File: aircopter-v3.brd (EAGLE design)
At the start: 47 x 28 mm, 44 parts, among them IC1 STF202-22T1G, M1 WIRELESS-NRF24L01, U2 GY-521MPU6050, Y1 20 MHz

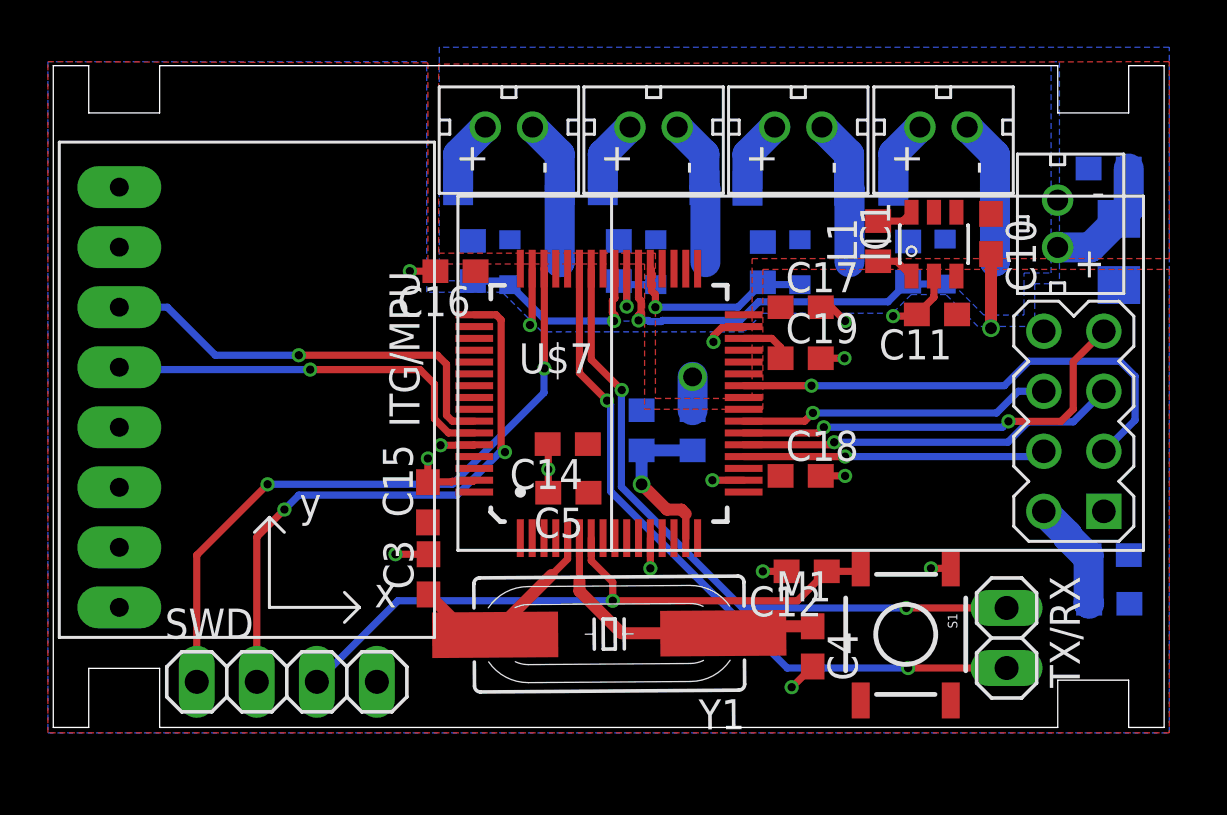
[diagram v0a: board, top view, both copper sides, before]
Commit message: redid motor section and planes, slightly moved mcu and radio, other small changes
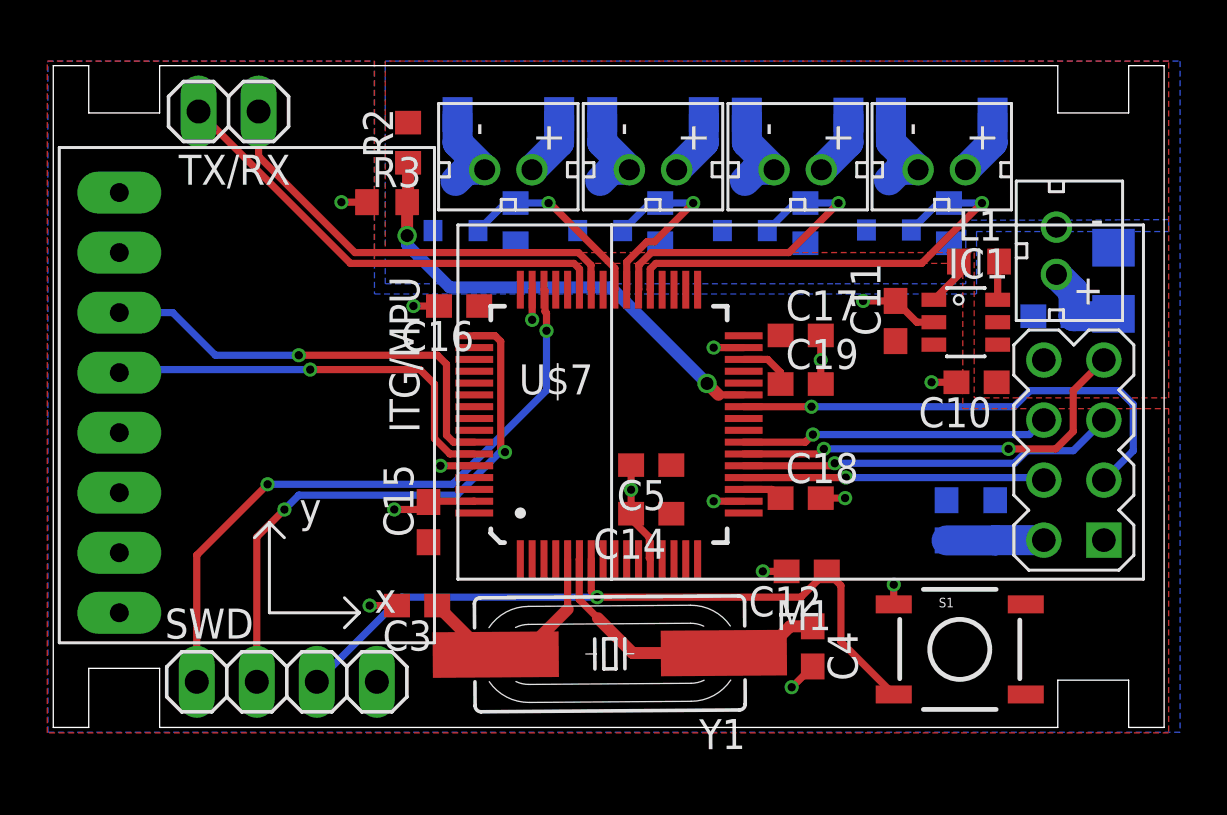
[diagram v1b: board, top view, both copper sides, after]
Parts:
- moved TX/RX 39.7 mm to (7.42, 26.1), turned to 180 degrees
- moved R2 17.1 mm to (15.0, 24.7), flipped to the top
- moved R3 14.5 mm to (14.1, 22.2), flipped to the top, turned to 0 degrees
- moved NMOS2 9.75 mm to (29.3, 22.0), turned to 0 degrees
- moved R1 8.05 mm to (37.9, 21.3), turned to 90 degrees
- moved C1 7.74 mm to (37.8, 8.76), turned to 90 degrees
- moved D2 6.93 mm to (31.5, 25.9), turned to 180 degrees
- moved D1 6.82 mm to (37.6, 25.9), turned to 180 degrees
- moved C13 6.67 mm to (42.3, 17.4)
- moved U$3 6.43 mm to (31.5, 23.6), turned to 270 degrees
- moved U$2 6.33 mm to (37.6, 23.6), turned to 270 degrees
- moved C10 6.30 mm to (39.1, 14.6), turned to 180 degrees
- moved C2 5.02 mm to (39.9, 8.76), turned to 90 degrees
- moved R4 4.64 mm to (31.8, 21.3), turned to 90 degrees
- moved C14 4.60 mm to (25.3, 9.04)
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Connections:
- net VDIV: now also U$7.27; no longer U$7.15
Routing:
- net VDIV: track 7.01 -> 20.4 mm, vias 1 -> 2
- net PWM1: track 8.31 -> 19.5 mm
- net RX: track 29.8 -> 19.8 mm, vias 2 -> 0
- net TX: track 28.2 -> 18.9 mm, vias 2 -> 0
- net PWM3: track 4.16 -> 8.49 mm
- net 3V7: track 19.0 -> 15.0 mm, vias 1 -> 0
- net RST: track 28.0 -> 31.6 mm
- net N$1: track 6.20 -> 4.21 mm
- net N$3: track 6.21 -> 4.25 mm
- net N$2: track 6.18 -> 4.22 mm
- net N$4: track 6.19 -> 4.25 mm
- net PWM2: track 16.0 -> 14.1 mm
- net GND: track 28.2 -> 27.0 mm, vias 17 -> 16
- net 3V3: track 4.77 -> 5.83 mm
- net SWCLK: track 25.0 -> 24.1 mm
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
